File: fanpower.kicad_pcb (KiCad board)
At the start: 2 copper layers, 25.4 x 44.2 mm, 21 parts, among them J2 Conn_01x03, Q1 BSH105,215, Q2 BSH105,215, SW1 SW_SPDT, SW2 SW_SPDT, U1 R-78E5.0-0.5

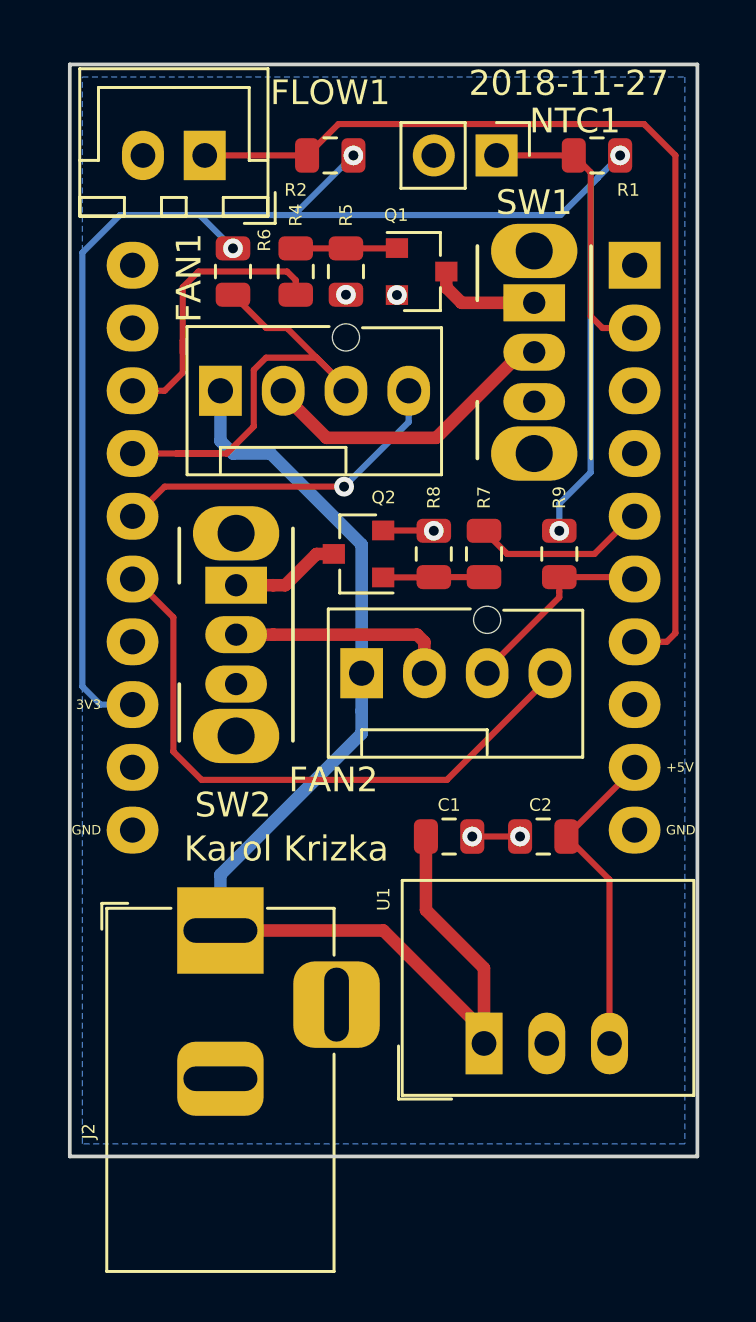
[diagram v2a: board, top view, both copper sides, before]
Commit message: Make board a bit longer.
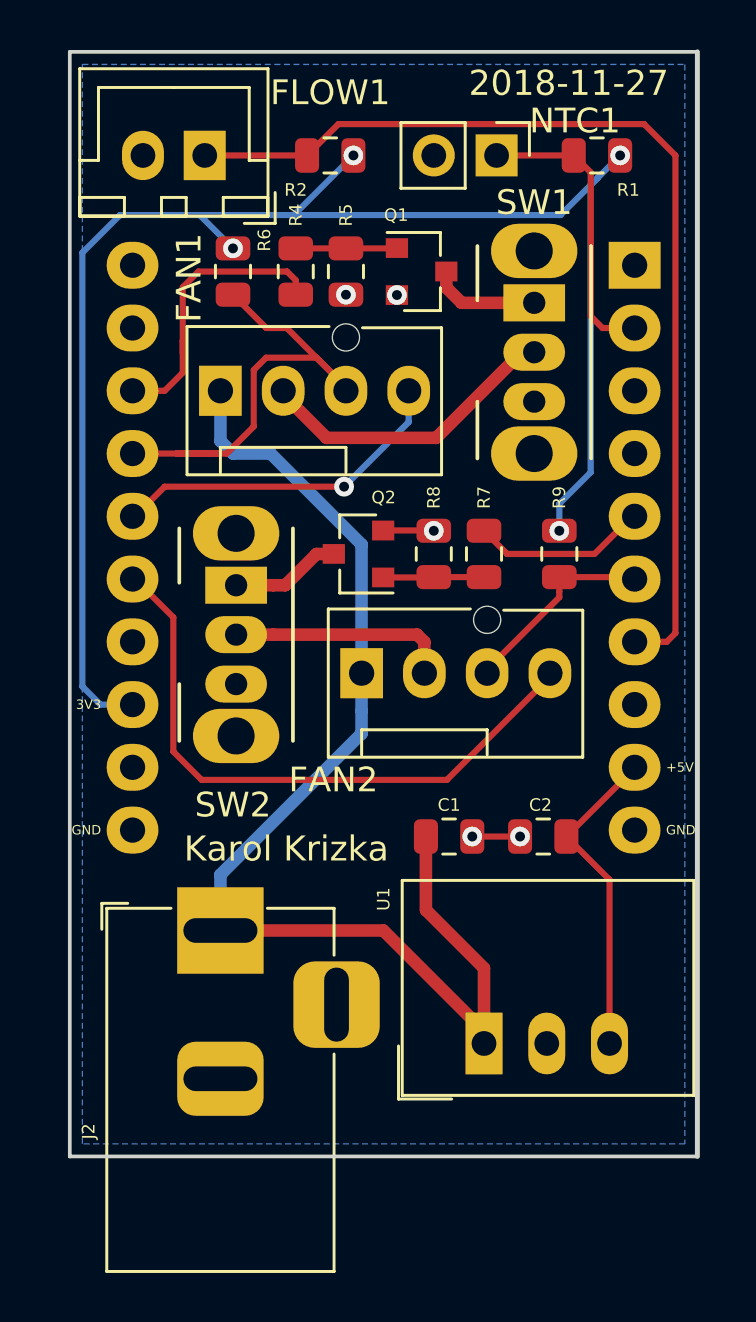
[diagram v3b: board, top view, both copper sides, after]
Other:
- board size 25.4 x 44.2 mm -> 25.4 x 44.7 mm
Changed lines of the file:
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@@
     )
   )
+  (gr_line (start 186.944 127.508) (end 186.944 82.804) (layer Edge.Cuts) (width 0.15))
+  (gr_line (start 212.344 82.804) (end 212.344 127.508) (layer Edge.Cuts) (width 0.2))
   (gr_text 2018-11-27 (at 207.137 84.074) (layer F.SilkS)
     (effects (font (size 1.016 1.016) (thickness 0.127)))
@@
     (effects (font (size 1.016 1.016) (thickness 0.127)))
   )
-  (gr_line (start 186.944 83.312) (end 186.944 127.508) (layer Edge.Cuts) (width 0.15))
   (gr_line (start 212.344 127.508) (end 186.944 127.508) (layer Edge.Cuts) (width 0.15))
-  (gr_line (start 212.344 83.312) (end 212.344 127.508) (layer Edge.Cuts) (width 0.15))
-  (gr_line (start 186.944 83.312) (end 212.344 83.312) (layer Edge.Cuts) (width 0.15))
+  (gr_line (start 186.944 82.804) (end 212.344 82.804) (layer Edge.Cuts) (width 0.15))
   (gr_text 3V3 (at 188.214 109.22) (layer F.SilkS)
     (effects (font (size 0.381 0.381) (thickness 0.0762)) (justify right))
@@
   (segment (start 195.738 91.694) (end 192.151 91.694) (width 0.25) (layer F.Cu) (net 7))
   (segment (start 192.151 91.694) (end 191.516 92.329) (width 0.25) (layer F.Cu) (net 7))
-  (segment (start 189.584 101.6) (end 189.484 101.6) (width 0.25) (layer F.Cu) (net 8))
-  (segment (start 198.045 100.4) (end 190.784 100.4) (width 0.25) (layer F.Cu) (net 8))
-  (segment (start 190.784 100.4) (end 189.584 101.6) (width 0.25) (layer F.Cu) (net 8))
   (segment (start 189.6595 96.52) (end 189.484 96.52) (width 0.25) (layer F.Cu) (net 7))
   (segment (start 189.584 96.52) (end 189.484 96.52) (width 0.25) (layer F.Cu) (net 7))
@@
   (segment (start 191.516 92.329) (end 191.516 94.488) (width 0.25) (layer F.Cu) (net 7))
   (segment (start 191.516 94.488) (end 191.516 94.996) (width 0.25) (layer F.Cu) (net 7))
+  (segment (start 189.584 101.6) (end 189.484 101.6) (width 0.25) (layer F.Cu) (net 8))
+  (segment (start 198.045 100.4) (end 190.784 100.4) (width 0.25) (layer F.Cu) (net 8))
+  (segment (start 190.784 100.4) (end 189.584 101.6) (width 0.25) (layer F.Cu) (net 8))
   (segment (start 200.66 96.52) (end 200.66 97.785) (width 0.25) (layer B.Cu) (net 8))
   (via (at 198.045 100.4) (size 0.8) (drill 0.4) (layers F.Cu B.Cu) (net 8))
@@
   (segment (start 206.8045 89.408) (end 208.3285 87.884) (width 0.25) (layer B.Cu) (net 14))
   (segment (start 208.3285 87.884) (end 209.2175 86.995) (width 0.25) (layer B.Cu) (net 14))
-  (segment (start 209.704 106.68) (end 209.804 106.68) (width 0.25) (layer F.Cu) (net 24))
   (segment (start 208.788 116.305782) (end 207.042696 114.560478) (width 0.25) (layer F.Cu) (net 15))
   (segment (start 208.788 122.936) (end 208.788 116.305782) (width 0.25) (layer F.Cu) (net 15))
   (segment (start 209.804 111.799174) (end 209.804 111.76) (width 0.25) (layer F.Cu) (net 15))
   (segment (start 207.042696 114.560478) (end 209.804 111.799174) (width 0.25) (layer F.Cu) (net 15))
-  (segment (start 203.708 122.436) (end 203.708 122.936) (width 0.508) (layer F.Cu) (net 18))
-  (segment (start 199.636 118.364) (end 203.708 122.436) (width 0.508) (layer F.Cu) (net 18))
-  (segment (start 193.04 118.364) (end 199.636 118.364) (width 0.508) (layer F.Cu) (net 18))
-  (segment (start 201.357696 114.560478) (end 201.357696 117.537696) (width 0.508) (layer F.Cu) (net 18))
-  (segment (start 203.708 119.888) (end 203.708 122.936) (width 0.508) (layer F.Cu) (net 18))
-  (segment (start 201.357696 117.537696) (end 203.708 119.888) (width 0.508) (layer F.Cu) (net 18))
   (segment (start 201.8155 102.174) (end 201.803 102.1865) (width 0.25) (layer F.Cu) (net 17))
   (segment (start 201.6635 102.174) (end 201.676 102.1865) (width 0.25) (layer F.Cu) (net 17))
@@
   (via (at 203.232696 114.560478) (size 0.8) (drill 0.4) (layers F.Cu B.Cu) (net 17))
   (via (at 205.167696 114.560478) (size 0.8) (drill 0.4) (layers F.Cu B.Cu) (net 17))
+  (segment (start 203.708 122.436) (end 203.708 122.936) (width 0.508) (layer F.Cu) (net 18))
+  (segment (start 199.636 118.364) (end 203.708 122.436) (width 0.508) (layer F.Cu) (net 18))
+  (segment (start 193.04 118.364) (end 199.636 118.364) (width 0.508) (layer F.Cu) (net 18))
+  (segment (start 201.357696 114.560478) (end 201.357696 117.537696) (width 0.508) (layer F.Cu) (net 18))
+  (segment (start 203.708 119.888) (end 203.708 122.936) (width 0.508) (layer F.Cu) (net 18))
+  (segment (start 201.357696 117.537696) (end 203.708 119.888) (width 0.508) (layer F.Cu) (net 18))
   (segment (start 198.755 109.473) (end 198.755 107.95) (width 0.508) (layer B.Cu) (net 18))
   (segment (start 198.755 110.391) (end 198.755 109.473) (width 0.508) (layer B.Cu) (net 18))
@@
   (segment (start 193.04 98.552) (end 193.04 96.52) (width 0.508) (layer B.Cu) (net 18))
   (segment (start 193.548 99.06) (end 193.04 98.552) (width 0.508) (layer B.Cu) (net 18))
-  (segment (start 195.58 96.67) (end 197.335 98.425) (width 0.508) (layer F.Cu) (net 27))
-  (segment (start 195.58 96.52) (end 195.58 96.67) (width 0.508) (layer F.Cu) (net 27))
-  (segment (start 205.24 94.96) (end 205.74 94.96) (width 0.508) (layer F.Cu) (net 27))
-  (segment (start 201.775 98.425) (end 205.24 94.96) (width 0.508) (layer F.Cu) (net 27))
-  (segment (start 197.335 98.425) (end 201.775 98.425) (width 0.508) (layer F.Cu) (net 27))
-  (segment (start 195.175 106.39) (end 193.675 106.39) (width 0.508) (layer F.Cu) (net 26))
-  (segment (start 201.295 106.685) (end 201 106.39) (width 0.508) (layer F.Cu) (net 26))
-  (segment (start 201 106.39) (end 195.175 106.39) (width 0.508) (layer F.Cu) (net 26))
-  (segment (start 201.295 107.95) (end 201.295 106.685) (width 0.508) (layer F.Cu) (net 26))
   (segment (start 203.6955 104.074) (end 203.708 104.0615) (width 0.25) (layer F.Cu) (net 20))
   (segment (start 201.6635 104.074) (end 201.676 104.0615) (width 0.25) (layer F.Cu) (net 20))
@@
   (segment (start 196.928 103.124) (end 195.662 104.39) (width 0.508) (layer F.Cu) (net 23))
   (segment (start 197.628 103.124) (end 196.928 103.124) (width 0.508) (layer F.Cu) (net 23))
+  (segment (start 209.704 106.68) (end 209.804 106.68) (width 0.25) (layer F.Cu) (net 24))
   (segment (start 211.455 106.329) (end 211.104 106.68) (width 0.25) (layer F.Cu) (net 24))
   (segment (start 211.104 106.68) (end 209.804 106.68) (width 0.25) (layer F.Cu) (net 24))
@@
   (segment (start 196.5475 86.995) (end 197.8175 85.725) (width 0.25) (layer F.Cu) (net 24))
   (segment (start 192.405 86.995) (end 196.5475 86.995) (width 0.25) (layer F.Cu) (net 24))
+  (segment (start 195.175 106.39) (end 193.675 106.39) (width 0.508) (layer F.Cu) (net 26))
+  (segment (start 201.295 106.685) (end 201 106.39) (width 0.508) (layer F.Cu) (net 26))
+  (segment (start 201 106.39) (end 195.175 106.39) (width 0.508) (layer F.Cu) (net 26))
+  (segment (start 201.295 107.95) (end 201.295 106.685) (width 0.508) (layer F.Cu) (net 26))
+  (segment (start 195.58 96.67) (end 197.335 98.425) (width 0.508) (layer F.Cu) (net 27))
+  (segment (start 195.58 96.52) (end 195.58 96.67) (width 0.508) (layer F.Cu) (net 27))
+  (segment (start 205.24 94.96) (end 205.74 94.96) (width 0.508) (layer F.Cu) (net 27))
+  (segment (start 201.775 98.425) (end 205.24 94.96) (width 0.508) (layer F.Cu) (net 27))
+  (segment (start 197.335 98.425) (end 201.775 98.425) (width 0.508) (layer F.Cu) (net 27))
   (zone (net 17) (net_name GND) (layer B.Cu) (hatch edge 0.508)
     (connect_pads (clearance 0.508))
@@
     (polygon
       (pts
-        (xy 187.452 83.82) (xy 211.836 83.82) (xy 211.836 127) (xy 187.452 127)
+        (xy 187.452 83.312) (xy 211.836 83.312) (xy 211.836 127) (xy 187.452 127)
       )
     )

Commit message: Fix fan pinout. The +12V and GND were swapped.
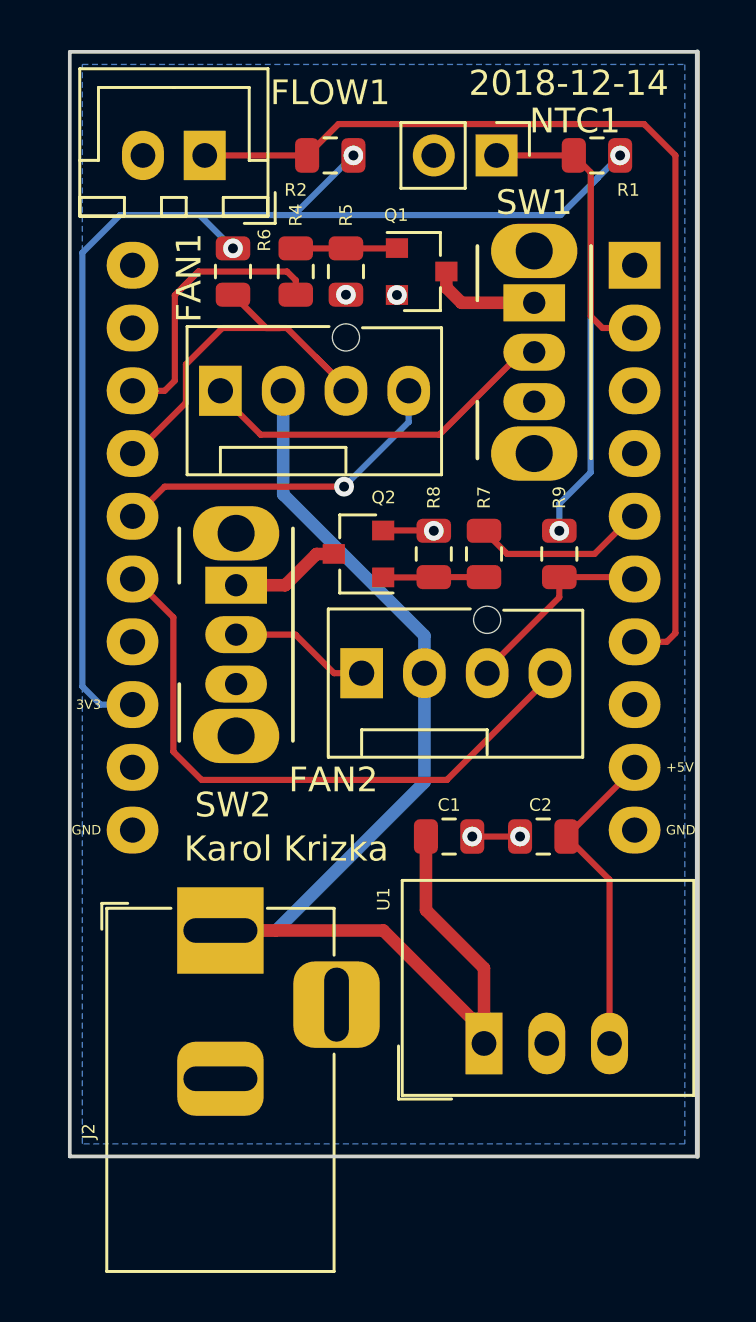
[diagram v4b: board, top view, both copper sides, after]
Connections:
- FAN1 pad 1: +12V -> Net-(FAN1-Pad1)
- FAN1 pad 2: Net-(FAN1-Pad2) -> +12V
- FAN2 pad 1: +12V -> Net-(FAN2-Pad1)
- FAN2 pad 2: Net-(FAN2-Pad2) -> +12V
- SW1 pad 2: Net-(FAN1-Pad2) -> Net-(FAN1-Pad1)
- SW2 pad 2: Net-(FAN2-Pad2) -> Net-(FAN2-Pad1)
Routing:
- net Net-(FAN1-Pad1): track 0.00 -> 14.9 mm
- net Net-(FAN1-Pad2): track 12.5 -> 0.00 mm
- net Net-(FAN2-Pad2): track 9.01 -> 0.00 mm
- net Net-(FAN2-Pad1): track 0.00 -> 5.73 mm
- net /SIGTACH1: track 20.2 -> 17.1 mm
- net +12V: track 49.7 -> 51.3 mm
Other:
- board text added: "2018-12-14"
- board text removed: "2018-11-27"
